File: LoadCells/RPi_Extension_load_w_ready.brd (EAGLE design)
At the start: 80 x 50 mm, 42 parts, among them U1 AD7730BRUZ, U2 AD7730BRUZ, U3 AD7730BRUZ, U4 AD7730BRUZ, U5 AD7730BRUZ, U6 AD7730BRUZ, U7 AD7730BRUZ, U8 AD7730BRUZ, U9 STM32F103RCT6, Y1 ABM3B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

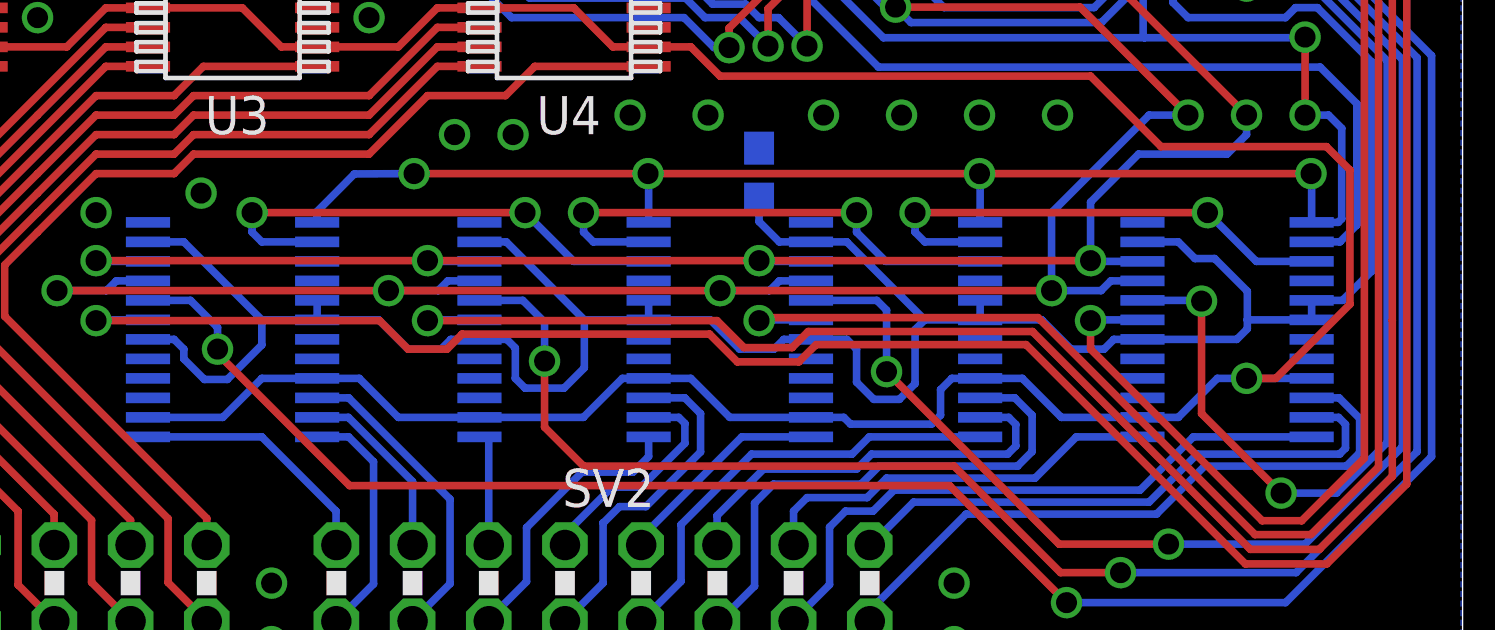
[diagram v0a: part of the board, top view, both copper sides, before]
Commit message: fixed severe bug on adc board
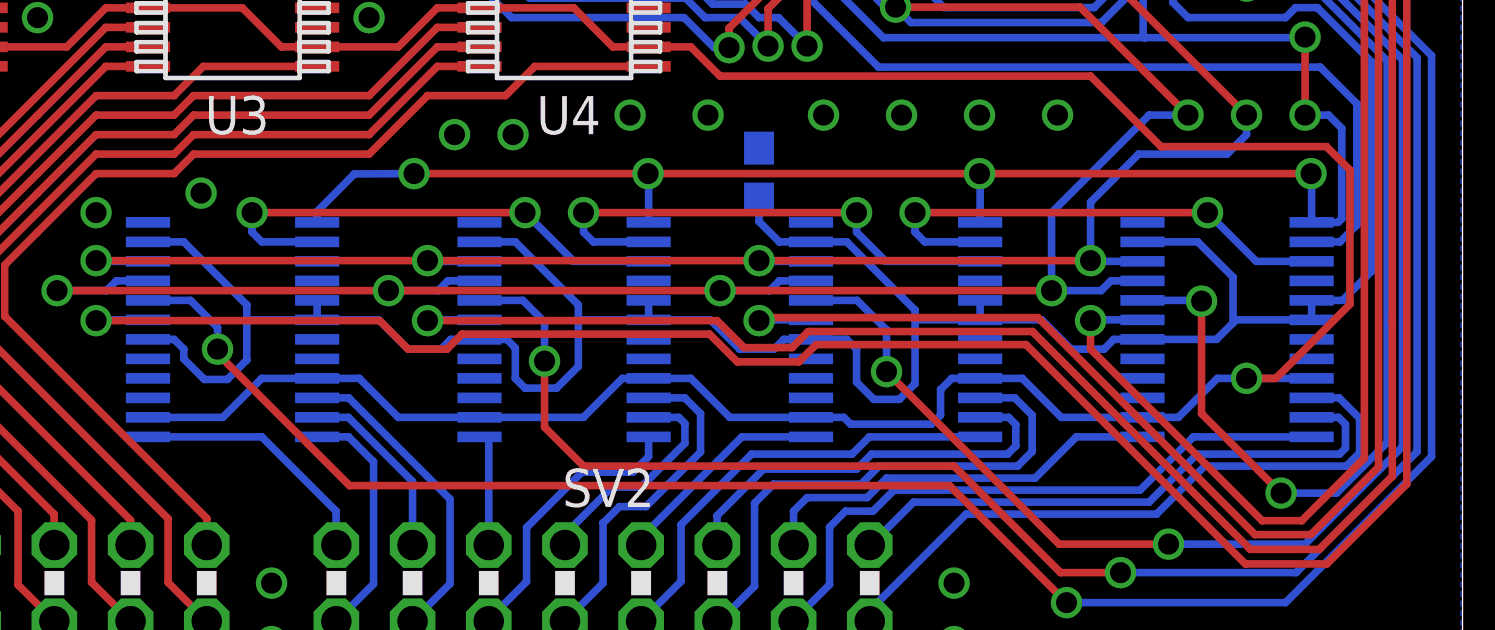
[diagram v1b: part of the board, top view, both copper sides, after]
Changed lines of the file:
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@@
 <via x="9.1" y="13.65" extent="1-16" drill="0.7"/>
 <via x="9.1" y="10.4" extent="1-16" drill="0.7"/>
+<wire x1="74.9694" y1="14.625" x2="74.9694" y2="12.025" width="0" layer="19" extent="16-16"/>
 </signal>
 <signal name="DVCC">
@@
 <contactref element="U5" pad="6"/>
 <contactref element="U5" pad="18"/>
-<wire x1="74.9694" y1="13.325" x2="72.825" y2="13.325" width="0.254" layer="16"/>
+<wire x1="74.9694" y1="13.325" x2="72.45" y2="13.325" width="0.254" layer="16"/>
 <wire x1="63.8408" y1="25.485" x2="63.8408" y2="28.0908" width="0.254" layer="16"/>
 <wire x1="76.67" y1="40.36" x2="76.67" y2="38.32" width="0.254" layer="16"/>
@@
 <contactref element="U6" pad="18"/>
 <wire x1="58.2806" y1="15.924996875" x2="59.475003125" y2="15.924996875" width="0.254" layer="16"/>
-<wire x1="59.475003125" y1="15.924996875" x2="62.075" y2="13.325" width="0.254" layer="16"/>
-<wire x1="63.9194" y1="13.325" x2="62.075" y2="13.325" width="0.254" layer="16"/>
+<wire x1="63.9194" y1="13.325" x2="61.75" y2="13.325" width="0.254" layer="16"/>
 <wire x1="63.9194" y1="13.975003125" x2="63.9194" y2="13.325" width="0.254" layer="16"/>
 <wire x1="63.9194" y1="13.325" x2="65.975" y2="13.325" width="0.254" layer="16"/>
@@
 <wire x1="41.8194" y1="13.325" x2="43.875" y2="13.325" width="0.254" layer="16"/>
 <wire x1="43.875" y1="13.325" x2="44.85" y2="12.35" width="0.254" layer="16"/>
-<wire x1="36.1806" y1="15.924996875" x2="37.375003125" y2="15.924996875" width="0.254" layer="16"/>
-<wire x1="37.375003125" y1="15.924996875" x2="39.975" y2="13.325" width="0.254" layer="16"/>
-<wire x1="41.8194" y1="13.325" x2="39.975" y2="13.325" width="0.254" layer="16"/>
-<wire x1="52.8694" y1="13.325" x2="50.725" y2="13.325" width="0.254" layer="16"/>
+<wire x1="41.8194" y1="13.325" x2="39.475" y2="13.325" width="0.254" layer="16"/>
+<wire x1="52.8694" y1="13.325" x2="50.525" y2="13.325" width="0.254" layer="16"/>
 <wire x1="47.2306" y1="12.675" x2="48.13995625" y2="12.675" width="0.254" layer="16"/>
 <wire x1="48.13995625" y1="12.675" x2="48.425" y2="12.38995625" width="0.254" layer="16"/>
@@
 <wire x1="75.2606" y1="28.9394" x2="75.9" y2="28.3" width="0.254" layer="16"/>
 <wire x1="75.9" y1="28.3" x2="76.65" y2="28.3" width="0.254" layer="16"/>
-<wire x1="39.975" y1="13.325" x2="39.975" y2="12.48965" width="0.254" layer="16"/>
-<wire x1="39.975" y1="12.48965" x2="38.8244" y2="11.33905" width="0.254" layer="16"/>
+<wire x1="39.475" y1="13.325" x2="39.475" y2="11.98965" width="0.254" layer="16"/>
 <wire x1="38.8244" y1="11.33905" x2="38.060953125" y2="11.33905" width="0.254" layer="16"/>
 <wire x1="38.060953125" y1="11.33905" x2="37.375" y2="12.025" width="0.254" layer="16"/>
 <wire x1="48.425" y1="11.375" x2="48.75" y2="11.05" width="0.254" layer="16"/>
-<wire x1="48.75" y1="11.05" x2="50.05" y2="11.05" width="0.254" layer="16"/>
-<wire x1="50.725" y1="13.325" x2="50.725" y2="11.725" width="0.254" layer="16"/>
-<wire x1="50.725" y1="11.725" x2="50.05" y2="11.05" width="0.254" layer="16"/>
-<wire x1="47.2306" y1="15.924996875" x2="48.125003125" y2="15.924996875" width="0.254" layer="16"/>
-<wire x1="48.125003125" y1="15.924996875" x2="50.725" y2="13.325" width="0.254" layer="16"/>
+<wire x1="50.525" y1="13.325" x2="50.525" y2="11.775" width="0.254" layer="16"/>
 <wire x1="58.2806" y1="12.675" x2="59.475" y2="12.675" width="0.254" layer="16"/>
 <wire x1="59.475" y1="12.675" x2="59.8" y2="12.35" width="0.254" layer="16"/>
@@
 <wire x1="60.374265625" y1="10.675734375" x2="61.225734375" y2="10.675734375" width="0.254" layer="16"/>
 <wire x1="61.225734375" y1="10.675734375" x2="61.75" y2="11.2" width="0.254" layer="16"/>
-<wire x1="61.75" y1="11.2" x2="61.75" y2="13" width="0.254" layer="16"/>
-<wire x1="61.75" y1="13" x2="62.075" y2="13.325" width="0.254" layer="16"/>
-<wire x1="69.3306" y1="12.675" x2="72.475" y2="12.675" width="0.254" layer="16"/>
-<wire x1="72.825" y1="13.325" x2="72.825" y2="14.27993125" width="0.254" layer="16"/>
-<wire x1="72.825" y1="14.27993125" x2="71.735728125" y2="15.369203125" width="0.254" layer="16"/>
-<wire x1="70.525003125" y1="15.924996875" x2="69.3306" y2="15.924996875" width="0.254" layer="16"/>
-<wire x1="72.825" y1="13.325" x2="72.825" y2="13.025" width="0.254" layer="16"/>
-<wire x1="72.825" y1="13.025" x2="72.475" y2="12.675" width="0.254" layer="16"/>
-<wire x1="70.525003125" y1="15.924996875" x2="71.080796875" y2="15.369203125" width="0.254" layer="16"/>
-<wire x1="71.735728125" y1="15.369203125" x2="71.080796875" y2="15.369203125" width="0.254" layer="16"/>
+<wire x1="69.3306" y1="12.675" x2="71.8" y2="12.675" width="0.254" layer="16"/>
+<wire x1="71.175003125" y1="15.924996875" x2="69.3306" y2="15.924996875" width="0.254" layer="16"/>
+<wire x1="71.175003125" y1="15.924996875" x2="72.35" y2="14.75" width="0.254" layer="16"/>
+<wire x1="72.35" y1="14.75" x2="72.35" y2="13.225" width="0.254" layer="16"/>
+<wire x1="72.35" y1="13.225" x2="71.8" y2="12.675" width="0.254" layer="16"/>
+<wire x1="72.45" y1="13.325" x2="72.35" y2="13.225" width="0.254" layer="16"/>
+<wire x1="59.475003125" y1="15.924996875" x2="61.75" y2="13.65" width="0.254" layer="16"/>
+<wire x1="61.75" y1="13.65" x2="61.75" y2="13.325" width="0.254" layer="16"/>
+<wire x1="61.75" y1="11.2" x2="61.75" y2="13.325" width="0.254" layer="16"/>
+<wire x1="48.75" y1="11.05" x2="49.8" y2="11.05" width="0.254" layer="16"/>
+<wire x1="49.8" y1="11.05" x2="50.525" y2="11.775" width="0.254" layer="16"/>
+<wire x1="47.2306" y1="15.924996875" x2="48.425003125" y2="15.924996875" width="0.254" layer="16"/>
+<wire x1="48.425003125" y1="15.924996875" x2="50.525" y2="13.825" width="0.254" layer="16"/>
+<wire x1="50.525" y1="13.325" x2="50.525" y2="13.825" width="0.254" layer="16"/>
+<wire x1="39.475" y1="11.98965" x2="38.8244" y2="11.33905" width="0.254" layer="16"/>
+<wire x1="36.1806" y1="15.924996875" x2="37.375003125" y2="15.924996875" width="0.254" layer="16"/>
+<wire x1="37.375003125" y1="15.924996875" x2="39.475" y2="13.825" width="0.254" layer="16"/>
+<wire x1="39.475" y1="13.325" x2="39.475" y2="13.825" width="0.254" layer="16"/>
 </signal>
 <signal name="MISO">
@@
 <signal name="RDY6">
 <contactref element="U6" pad="20"/>
-<wire x1="58.2806" y1="13.975" x2="60.475" y2="13.975" width="0.254" layer="16"/>
-<wire x1="60.475" y1="13.975" x2="60.8" y2="13.65" width="0.254" layer="16"/>
-<wire x1="60.8" y1="13.65" x2="60.8" y2="11.6" width="0.254" layer="16"/>
+<wire x1="58.2806" y1="13.975" x2="59.81606875" y2="13.975" width="0.254" layer="16"/>
+<wire x1="59.81606875" y1="13.975" x2="60.8" y2="12.99106875" width="0.254" layer="16"/>
+<wire x1="60.8" y1="12.99106875" x2="60.8" y2="11.6" width="0.254" layer="16"/>
 <via x="60.8" y="11.6" extent="1-16" drill="0.7"/>
 <contactref element="U9" pad="16"/>

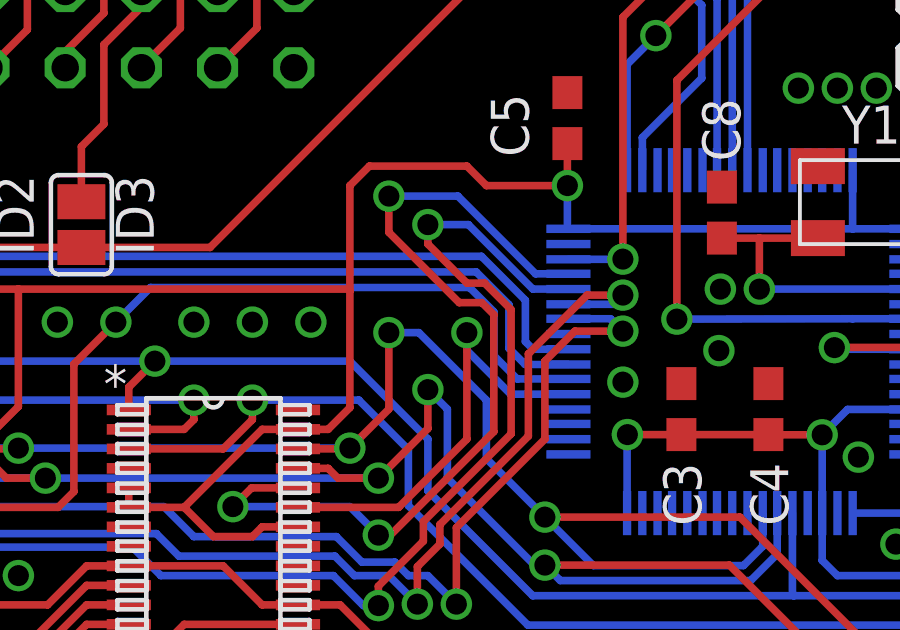
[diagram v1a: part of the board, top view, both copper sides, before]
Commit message: minor rerouting to remove useless corners
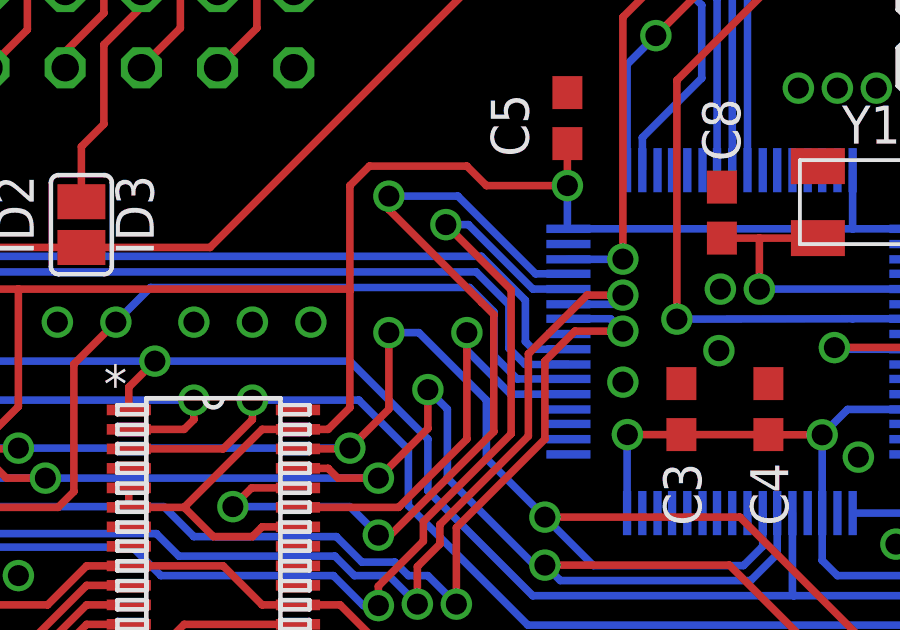
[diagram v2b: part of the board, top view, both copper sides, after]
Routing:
- net RDY1: track 63.4 -> 62.2 mm
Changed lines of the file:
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@@
 <wire x1="57.05" y1="24.55" x2="57.05" y2="25.2" width="0.254" layer="1"/>
 <wire x1="57.05" y1="25.2" x2="59.974609375" y2="28.124609375" width="0.254" layer="1"/>
-<wire x1="59.974609375" y1="32.2666375" x2="59.091246875" y2="33.15" width="0.254" layer="1"/>
-<wire x1="59.091246875" y1="33.15" x2="58.5" y2="33.15" width="0.254" layer="1"/>
 <contactref element="U9" pad="44"/>
 <wire x1="61.885" y1="32.9526" x2="60.6974" y2="32.9526" width="0.254" layer="16"/>
 <wire x1="60.6974" y1="32.9526" x2="58.55" y2="35.1" width="0.254" layer="16"/>
-<wire x1="58.5" y1="33.15" x2="57.2" y2="34.45" width="0.254" layer="1"/>
-<wire x1="57.2" y1="34.45" x2="57.2" y2="35.1" width="0.254" layer="1"/>
-<via x="57.2" y="35.1" extent="1-16" drill="0.7"/>
-<wire x1="57.2" y1="35.1" x2="58.55" y2="35.1" width="0.254" layer="16"/>
-<wire x1="59.974609375" y1="32.2666375" x2="59.974609375" y2="28.124609375" width="0.254" layer="1"/>
+<via x="57.8" y="35.1" extent="1-16" drill="0.7"/>
+<wire x1="57.8" y1="35.1" x2="58.55" y2="35.1" width="0.254" layer="16"/>
+<wire x1="59.974609375" y1="32.925390625" x2="59.974609375" y2="28.124609375" width="0.254" layer="1"/>
 <wire x1="55.55" y1="22.4" x2="55.05" y2="22.4" width="0.254" layer="16"/>
 <wire x1="55.05" y1="22.4" x2="54.05" y2="23.4" width="0.254" layer="16"/>
+<wire x1="59.974609375" y1="32.925390625" x2="57.8" y2="35.1" width="0.254" layer="1"/>
 </signal>
 <signal name="RDY8">
@@
 <wire x1="60.7894" y1="33.4606" x2="58.2" y2="36.05" width="0.254" layer="16"/>
 <wire x1="59.39828125" y1="32.10171875" x2="59" y2="32.5" width="0.254" layer="1"/>
-<wire x1="59" y1="32.5" x2="58.24360625" y2="32.5" width="0.254" layer="1"/>
-<wire x1="58.24360625" y1="32.5" x2="55.9" y2="34.84360625" width="0.254" layer="1"/>
-<wire x1="55.9" y1="34.84360625" x2="55.9" y2="36.05" width="0.254" layer="1"/>
+<wire x1="59" y1="32.5" x2="55.9" y2="35.6" width="0.254" layer="1"/>
+<wire x1="55.9" y1="35.6" x2="55.9" y2="36.05" width="0.254" layer="1"/>
 <via x="55.9" y="36.05" extent="1-16" drill="0.7"/>
 <wire x1="55.9" y1="36.05" x2="58.2" y2="36.05" width="0.254" layer="16"/>
